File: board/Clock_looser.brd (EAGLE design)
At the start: 50 x 50 mm, 17 parts

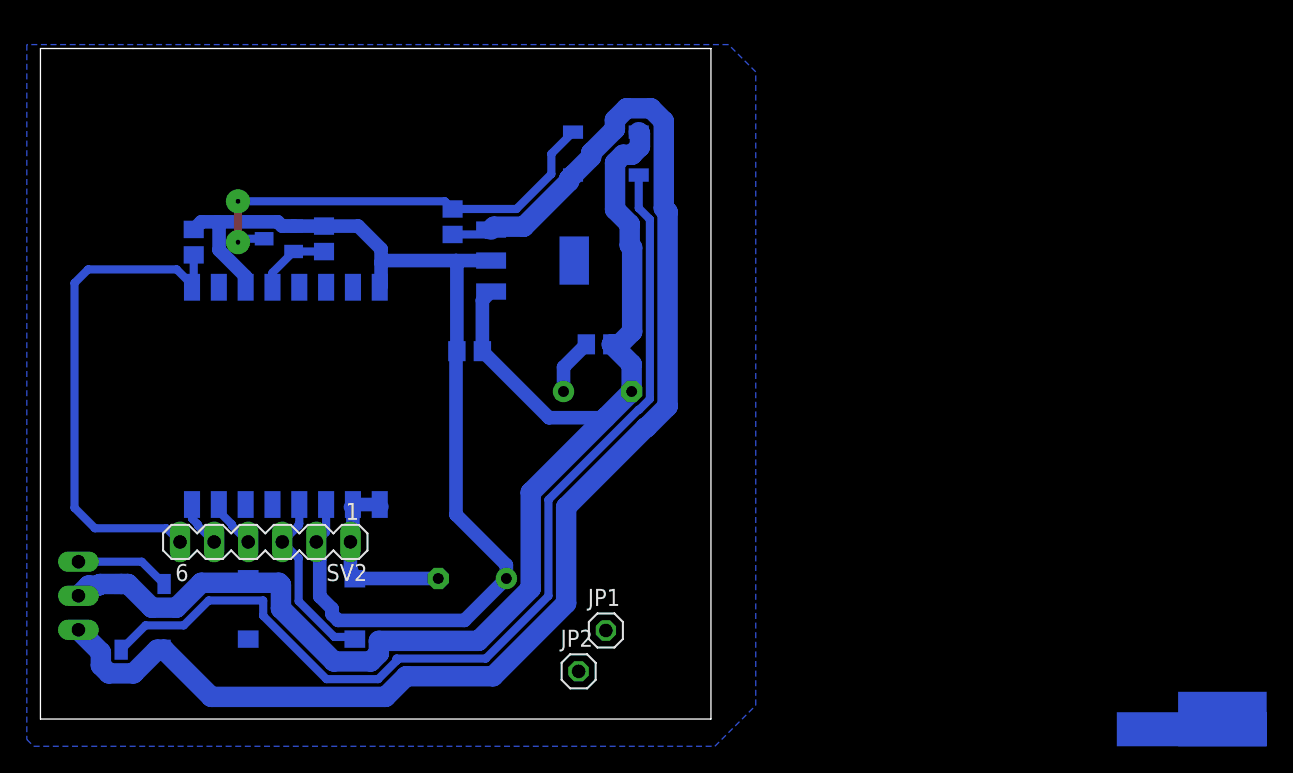
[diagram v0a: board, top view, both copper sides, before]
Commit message: Added LEDs and a photoresistor
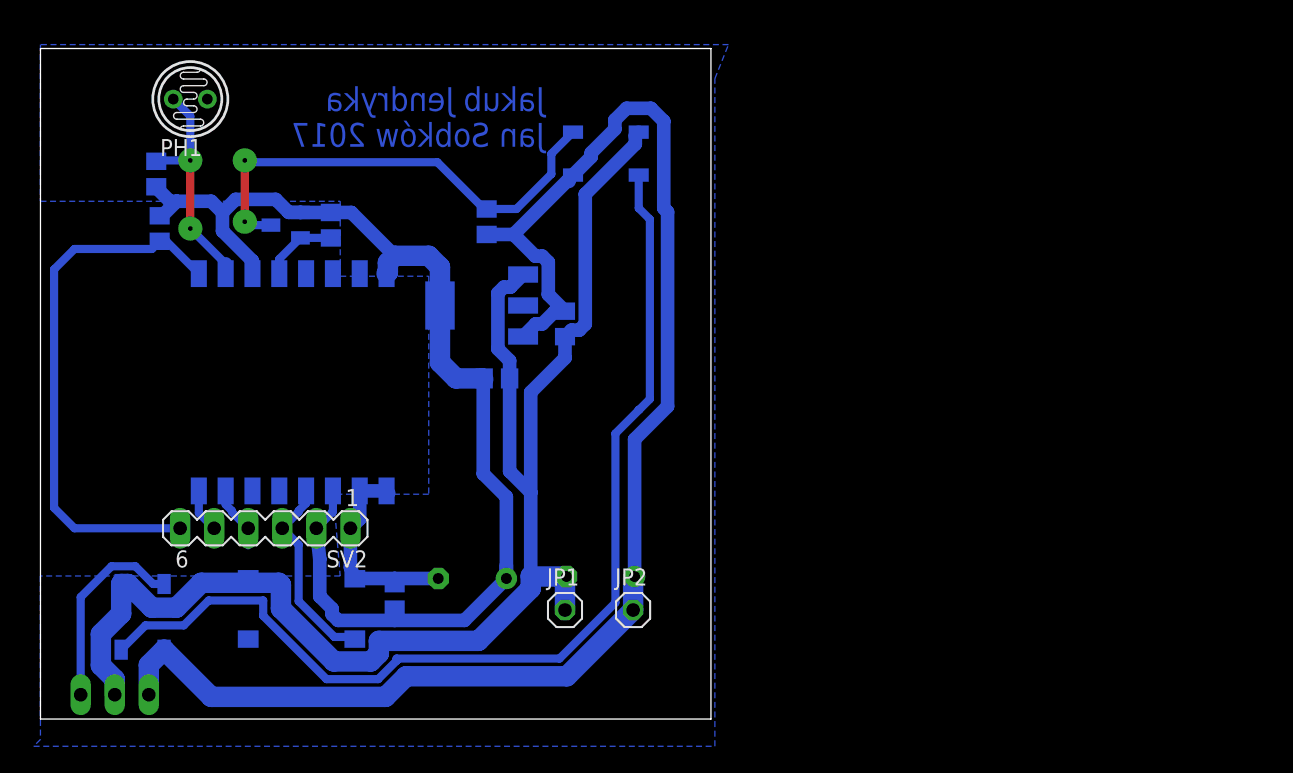
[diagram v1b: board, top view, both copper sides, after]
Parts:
- added C5: (no value), rcl:C0805
- added PH1: VT20N1, photo-elements:TO46-VT200
- added R4: (no value), rcl:R0805
- moved C1 13.8 mm to (41.8, 10.6), turned to 0 degrees
- moved SV1 7.86 mm to (5.54, 1.81), turned to 180 degrees
- moved JP2 6.12 mm to (44.2, 8.13)
- moved AMS1117 5.08 mm to (32.9, 30.8), turned to 270 degrees
- moved JP1 3.41 mm to (39.1, 8.13)
- moved C3 2.96 mm to (39.1, 29.5), turned to 270 degrees
- moved C4 2.87 mm to (34.0, 25.4)
- moved R3 2.74 mm to (8.89, 36.6)
- moved R2 2.54 mm to (33.3, 37.1)
- moved U$1 1.14 mm to (27.8, 33.2)
- moved R1 1.14 mm to (21.7, 36.8)
- moved U$2 1.14 mm to (18.3, 36.8)
- moved SV2 1.02 mm to (16.8, 14.2)
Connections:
- new net ADC: PH1.1, R4.1, U$1.10
- net GND: now also C5.2, PH1.2
- net VCC: now also C5.1, R4.2
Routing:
- net ADC: track 0.00 -> 17.6 mm, vias 0 -> 2
- net GND: track 112.7 -> 124.6 mm
- net N$2: track 7.08 -> 15.0 mm
- net VCC: track 80.7 -> 86.2 mm
- net N$1: track 74.0 -> 77.3 mm
- net REST: track 38.0 -> 40.8 mm
- net +5V: track 107.5 -> 110.4 mm
- net N$7: track 33.6 -> 35.9 mm
- net PRG_EN: track 13.6 -> 14.8 mm
- net RXD: track 4.08 -> 4.76 mm
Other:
- board text added: "Jakub Jendryka Jan Sobków 2017"

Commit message: Improved clearance
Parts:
- C1, C2: value (none) -> 100uF
- C3, C4, C5: value (none) -> 10nF
- R1, R2, R3: value (none) -> 10k
- SV1: value (none) -> LED strip
- SV2: value (none) -> Programmer
- moved PH1 8.14 mm to (3.05, 46.7), turned to 180 degrees
- moved C3 1.02 mm to (40.1, 29.5)
- moved R3 0.25 mm to (8.64, 36.6)
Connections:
- net N$9 renamed GPIO16
- net GND: now also S1.3
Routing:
- net GND: track 124.6 -> 119.3 mm
- net +5V: track 110.4 -> 113.3 mm
- net VCC: track 86.2 -> 88.0 mm
- net ADC: track 17.6 -> 19.0 mm
- net RXD: track 4.76 -> 3.49 mm
- net PRG_EN: track 14.8 -> 15.8 mm
- added copper zone on layer 16, net N$3
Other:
- board text added: "-"
- board text added: "5V"
